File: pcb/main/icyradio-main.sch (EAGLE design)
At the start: 689 parts, among them CON101 FPC-22P, CON1101 2EDG-2P-5MM-H, CON801 PCIE-X4-EDGE, J101 RJ45_MAG_LED_1G-TE-1-2301994-0, J701 TRSJACK, J702 TRSJACK, J703 TRSJACK, M701 SPH0641LM4H-1, M702 SPH0641LM4H-1, Q101 AO3400, Q1101 AO4805, Q1102 AO3400, Q1103 AO3400, Q1104 AO4805, Q1105 AO4805, Q1106 AO3400, T501 UWB1-85E, T502 UWB1-85E, T503 UWB1-85E, T504 UWB1-85E, T505 UWB1-85E, T506 UWB1-85E, T507 UWB1-85E, T508 UWB1-85E, U1001 LTC4313-3, U1002 UPD301C, U1003 MIC2019, U101 MIC2019, U102 RPI-CM4, U1101 MCP1804-3302, U1102 LT7182S, U1201 ADM7172ACPZ-5.0, U1202 ADM7171ACPZ-1.3, U1203 ADM7171ACPZ-3.3, U1204 MIC23159, U1205 MIC5166, U1206 ADM7171ACPZ-1.3, U1207 ADM7171ACPZ-3.3, U1208 MIC23159, U1209 MIC23155, U1210 ADP7142AUJZ-3.3, U1211 ADP150UJZ-1.8, U201 XC7A100TFGG484, U301 MT41K256M16TW-125, U302 MT41K256M16TW-125, U303 DSC1203DA3-333M3333, U401 AD9361, U402 LTC6957-3, U403 TG2520SMN-40.0000M, U501 MIC2019, U502 MIC2019, U503 MIC2019, U504 MIC2019, U505 ADL5601, U506 ADL5601, U601 8V97003, U701 ADAU1372, U901 74LVC1G157, U902 DSB321SDA, U903 SI5351C-B-GM

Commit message: PCB Work
Signed-off-by: João Silva <jgc3silva@gmail.com>
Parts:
- removed R1122, R1123: 10K Ohms, Resistor:RESISTOR-0402
- added C1: 100nF, Capacitor:CAPACITOR-0402
- added D2, D3, D4: LED0603, LED:LED0603
- added R1: 22 Ohms, Resistor:RESISTOR-0402
- added R10, R8, R9: 1K Ohms, Resistor:RESISTOR-0402
- added R2: 2.4K Ohms, Resistor:RESISTOR-0402
- added R3, R4, R5, R6, R7: 4.7K Ohms, Resistor:RESISTOR-0402
- added U1: SST26VF064B, Microchip:SST26VF064B
- C102, C1114, C1126, C1128, C1213, C1214, C1216, C1217, C1218, C1219, C1220, C1222, C1233, C1234, C1235, C1236, C1238, C1239, C1241, C1242, C1254, C1255, C410, C534, C535, C605, C608, C611, C612, C613, C701, C706, C708, C721, C722: device Capacitor:CAPACITOR-0603 -> Capacitor:CAPACITOR-0402
- C1259: value 4.7uF -> 10uF; device Capacitor:CAPACITOR-0603 -> Capacitor:CAPACITOR-0402
- R1210, R1215, R1216, R401: device Resistor:RESISTOR-0603 -> Resistor:RESISTOR-0402
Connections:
- net N$124 renamed VIN_REG_WP
- net N$125 renamed VIN_REG_RUN0
- net N$19 renamed VIN_REG_ASEL
- removed net !1V0_FAULT: R1123.1, U1102.1.!FAULT
- removed net !5V0_FAULT: R1122.1, U1102.0.!FAULT
- new net !FPGA_FLASH_CS: R2.1, U1.!CS!, U201.BANK14.IO_L6P/T0/!FCS
- new net !FPGA_INIT: D4.A, R10.1, R6.1, U201.BANK0-CFG.!INIT
- new net !FPGA_PROGRAM: R7.1, TC201-9(TRST).S, U201.BANK0-CFG.!PROGRAM
- new net FPGA_DONE: D3.A, R9.1, U201.BANK0-CFG.DONE
- new net FPGA_FLASH_IO0: U1.MOSI/IO0, U201.BANK14.IO_L1P/T0/D0/MOSI
- new net FPGA_FLASH_IO1: U1.MISO/IO1, U201.BANK14.IO_L1N/T0/D1/DIN
- new net FPGA_FLASH_IO2: R3.1, U1.!WP!/IO2, U201.BANK14.IO_L2P/T0/D2
- new net FPGA_FLASH_IO3: R4.1, U1.!HOLD!/IO3, U201.BANK14.IO_L2N/T0/D3
- new net FPGA_FLASH_SCK: U1.SCK, U201.BANK0-CFG.CCLK, U201.BANK14.IO_L23P/T3/A3/D19
- new net FPGA_JTAG_EN: R5.2, TC201-10(!RESET!).S, U201.BANK0-CFG.M2
- new net N$19: D2.A, R8.1
- new net TRX_SYNC_IN: R1.2, U201.BANK16.IO_L15P/T2_DQS, U401.INTERFACE.SYNC_IN
- net 2V5: now also U201.BANK16.IO_25, U201.BANK16.IO_L18N/T2, U201.BANK16.IO_L5N/T0, U201.BANK16.IO_L6N/T0/VREF
- net 3V3: now also C1.C1, R10.2, R2.2, R3.2, R4.2, R6.2, R7.2, R9.2, U1.VCC, U201.BANK0-CFG.M0
- net 3V5_VIN_REG_DRVCC: now also U1102.0.!FAULT, U1102.1.!FAULT; no longer R1122.2, R1123.2
- net GND: now also C1.C2, D2.C, D3.C, D4.C, R5.1, U1.GND, U201.BANK0-CFG.DXN, U201.BANK0-CFG.DXP, U201.BANK0-CFG.M1, U201.BANK14.IO_L3P/T0_DQS/!PUDC, U201.BANK15.IO_L10P/T1/AD11P, U201.BANK15.IO_L12N/T1/MRCC, U201.BANK15.IO_L18N/T2/A23, U201.BANK15.IO_L8P/T1/AD10P; no longer U401.INTERFACE.SYNC_IN
- net TRX_CTRL_OUT3: now also U201.BANK16.IO_L12P/T1/MRCC; no longer U201.BANK16.IO_L15N/T2_DQS
- net TRX_ENABLE: now also U201.BANK16.IO_L2P/T0; no longer U201.BANK16.IO_L15P/T2_DQS
- net TRX_EN_AGC: now also U201.BANK16.IO_0; no longer U201.BANK16.IO_L2P/T0
- net TRX_TX/!RX: now also U201.BANK16.IO_L1N/T0; no longer U201.BANK16.IO_0
- net VBUS: now also Q1101.2.D; no longer Q1101.1.D
- net VIN: now also Q1101.1.D; no longer Q1101.2.D
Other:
- moved on the sheet: Q1101.1, Q1101.2, R1119, R1120, TC201-1(VTARGET), U201.BANK0-CFG, U201.BANK0-XADC

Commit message: PCB Work
Signed-off-by: João Silva <jgc3silva@gmail.com>
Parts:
- added C2: 1uF, Capacitor:CAPACITOR-0402
- added CON1: FPC-22P, Generic Connector:FPC-22P
- added R11, R12: 2.2K Ohms, Resistor:RESISTOR-0402
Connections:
- net CM4_CAM_SCL renamed CM4_CAM1_SCL
- net CM4_CAM_SDA renamed CM4_CAM1_SDA
- net N$100 renamed SYNTH_RFOUTB_ACC_N
- net N$102 renamed SYNTH_RFOUTA_ACC_N
- net N$103 renamed SYNTH_RFOUTA_BIAS
- net N$104 renamed SYNTH_RFOUTA_N
- net N$105 renamed SYNTH_VTUNE
- net N$106 renamed SYNTH_RFOUTA_P
- net N$107 renamed SYNTH_RFOUTB_N
- net N$108 renamed SYNTH_RFOUTB_P
- net N$109 renamed SYNTH_CPOUT
- net N$33 renamed PCIE_SLOT_TX1_ACC_N
- net N$34 renamed PCIE_SLOT_TX1_ACC_P
- net N$35 renamed PCIE_SLOT_RX1_ACC_N
- net N$41 renamed PCIE_SLOT_RX1_ACC_P
- net N$43 renamed SYNTH_CPBIAS
- net N$45 renamed PCIE_SLOT_RX0_ACC_N
- net N$46 renamed PCIE_SLOT_RX0_ACC_P
- net N$51 renamed PCIE_CM4_RX_ACC_N
- net N$53 renamed PCIE_CM4_RX_ACC_P
- net N$63 renamed PCIE_SLOT_TX0_ACC_N
- net N$65 renamed PCIE_SLOT_TX0_ACC_P
- net N$68 renamed PCIE_CM4_TX_ACC_N
- net N$69 renamed PCIE_CM4_TX_ACC_P
- net N$75 renamed SYNTH_VREGVCO1
- net N$76 renamed SYNTH_VREGVCO2
- net N$77 renamed SYNTH_VREFVCO1
- net N$84 renamed SYNTH_VREFVCO2
- net N$85 renamed SYNTH_RFOUTB_BIAS
- net N$86 renamed SYNTH_RFOUTA_ACC_P
- net N$88 renamed SYNTH_REFIN_P
- net N$89 renamed SYNTH_REFIN_N
- net N$99 renamed SYNTH_RFOUTB_ACC_P
- new net CM4_CAM0_CSI_C_N: CON1-15.S, U102.CSI0.CAM_C_N
- new net CM4_CAM0_CSI_C_P: CON1-14.S, U102.CSI0.CAM_C_P
- new net CM4_CAM0_CSI_D0_N: CON1-21.S, U102.CSI0.CAM_D0_N
- new net CM4_CAM0_CSI_D0_P: CON1-20.S, U102.CSI0.CAM_D0_P
- new net CM4_CAM0_CSI_D1_N: CON1-18.S, U102.CSI0.CAM_D1_N
- new net CM4_CAM0_CSI_D1_P: CON1-17.S, U102.CSI0.CAM_D1_P
- new net CM4_CAM0_SCL: CON1-3.S, R12.1, U102.GPIO.GPIO1
- new net CM4_CAM0_SDA: CON1-2.S, R11.1, U102.GPIO.GPIO0
- net 3V3_CM4: now also C2.C1, CON1-1.S, R11.2, R12.2
- net CM4_CAM_GPIO: now also CON1-6.S
- net GND: now also C2.C2, CON1-10.S, CON1-13.S, CON1-16.S, CON1-19.S, CON1-22.S, CON1-4.S, CON1-7.S
- net TRX_DATA_CLK: now also U201.BANK15.IO_L13P/T2/MRCC; no longer U201.BANK15.IO_L12P/T1/MRCC
- net TRX_FB_CLK: now also U201.BANK15.IO_L12P/T1/MRCC; no longer U201.BANK15.IO_L13P/T2/MRCC
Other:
- note added: "1V8"
- note added: "CFGBVS = 1 -> Bank 0 at 3V3"
- note added: "DONE LED should light up after FPGA configuration. DONE LED is also controllable through STARTUPE2 primitive"
- note added: "Flash SCK is connecterd to CCLK for initial configuration, and also to a dedicated IO, to be used in the design at full speed."
- note added: "INIT LED should light up after FPGA housekeeping (during configuration)"
- note added: "It seems PTP is only working on one of these pins. To be tested in hardware."
- note added: "M[2:0} = 0b001 -> Boot from SPI Flash M[2:0} = 0b101 -> Boot from JTAG"
- note added: "Pullups as per Xillinx recommendation"
- moved on the sheet: D101, D102, Q101, R101, R104, R105, R106, R107, R110, TP13, TP14, U102.GPIO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

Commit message: PCB Work
Signed-off-by: João Silva <jgc3silva@gmail.com>
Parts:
- added C3: 1uF, Capacitor:CAPACITOR-0402
- added C4: 100nF, Capacitor:CAPACITOR-0402
- added FB1: 1uH, Inductor:FERRITE-0603
- added R13: 49.9 Ohms, Resistor:RESISTOR-0402
- R902, R904: value 100K Ohms -> 10K Ohms
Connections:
- new net N$34: C902.C1, C904.C1, C905.C1, FB1.2, U903.VDDOA, U903.VDDOB, U903.VDDOC, U903.VDDOD
- new net SYNTH_REF_CLK: C601.C1, R13.2
- net 3V3: now also C3.C1, FB1.1; no longer C902.C1, C904.C1, C905.C1, U903.VDDOA, U903.VDDOB, U903.VDDOC, U903.VDDOD
- net EXT_CLK_OUT: now also R912.1; no longer R911.1
- net GND: now also C3.C2, C4.C2, R13.1
- net SYNTH_REFIN_N: now also C4.C1
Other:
- moved on the sheet: C601, C902, C904, C905, C906, C907, C908, R601, R602, R603, R604, R605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

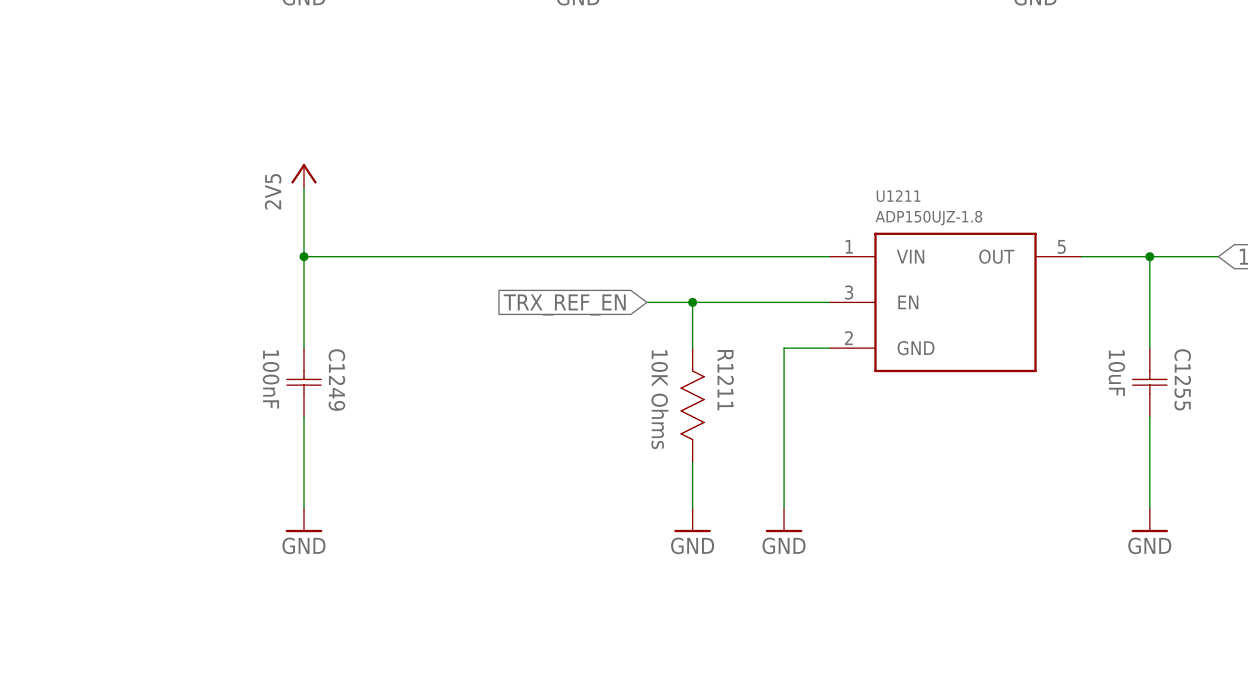
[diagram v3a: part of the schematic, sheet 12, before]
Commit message: Start DDR routing
Signed-off-by: João Silva <jgc3silva@gmail.com>
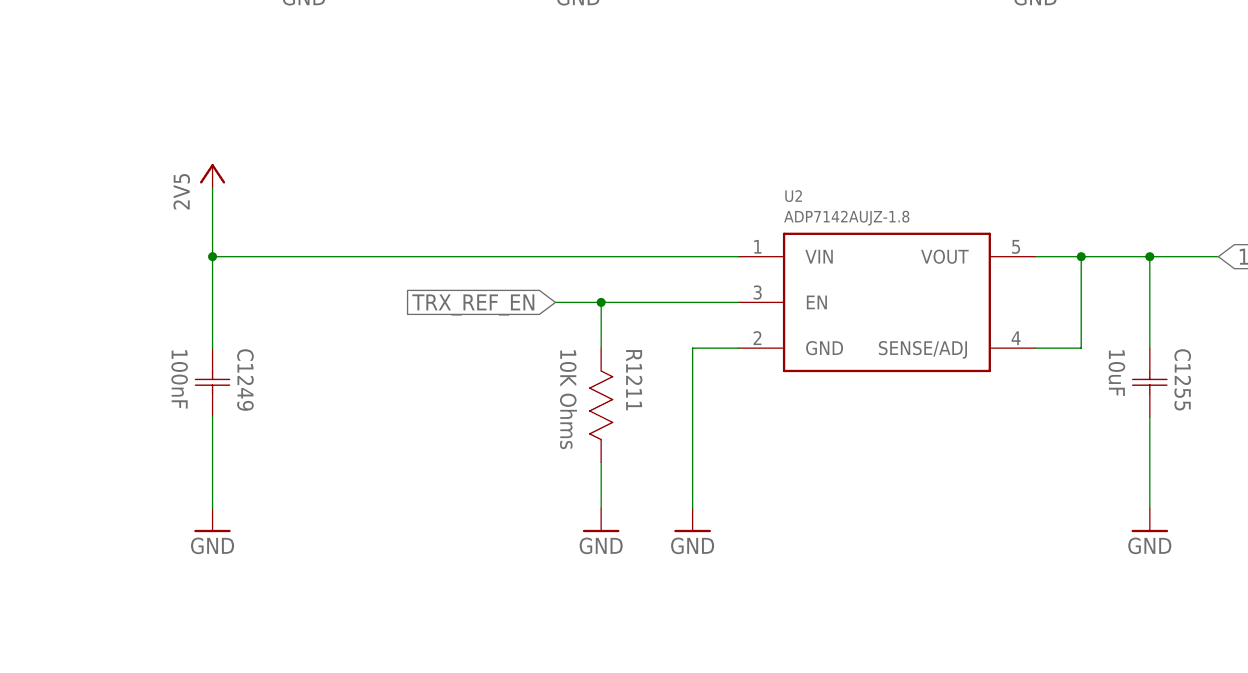
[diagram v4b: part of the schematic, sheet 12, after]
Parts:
- removed U1211: ADP150UJZ-1.8, Analog Devices:ADP150UJZ-1.8
- added U2: ADP7142AUJZ-1.8, Analog Devices:ADP7142AUJZ-1.8
- L1201, L1202, L1203, L1204, L1205: REF_COILCRAFT XGL3515-222ME -> (none)
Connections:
- new net CM4_UART_RXD: U102.GPIO.GPIO15
- new net CM4_UART_TXD: U102.GPIO.GPIO14
- new net CM4_WAKE: U102.GPIO.GPIO3
- net 1V8_TRX_REF: now also U2.SENSE/ADJ, U2.VOUT; no longer U1211.OUT
- net 2V5: now also U2.VIN; no longer U1211.VIN
- net GND: now also U2.GND; no longer U1211.GND
- net TRX_REF_EN: now also U2.EN; no longer U1211.EN
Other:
- moved on the sheet: C1249, R1211

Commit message: Remove second DDR3 chip as it was impossible to route with a 6-layer board Update HDL project to reflect hardware changes
Signed-off-by: João Silva <jgc3silva@gmail.com>
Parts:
- removed R301: 240 Ohms, Resistor:RESISTOR-0402
- removed R326: 40.2 Ohms, Resistor:RESISTOR-0402
- removed U301: MT41K256M16TW-125, Micron:MT41K256M16TW-125
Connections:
- removed net !DDR3_CS: R324.1, U201.BANK34.IO_L18N/T2, U301.!CS, U302.!CS
- removed net DDR3_DM2: U201.BANK35.IO_L19P/T3, U302.LDM
- removed net DDR3_DM3: U201.BANK34.IO_L1P/T0, U302.UDM
- removed net DDR3_DQ16: U201.BANK35.IO_L20P/T3, U302.DQ0
- removed net DDR3_DQ17: U201.BANK35.IO_L20N/T3, U302.DQ1
- removed net DDR3_DQ18: U201.BANK35.IO_L22P/T3, U302.DQ2
- removed net DDR3_DQ19: U201.BANK35.IO_L22N/T3, U302.DQ3
- removed net DDR3_DQ20: U201.BANK35.IO_L23P/T3, U302.DQ4
- removed net DDR3_DQ21: U201.BANK35.IO_L23N/T3, U302.DQ5
- removed net DDR3_DQ22: U201.BANK35.IO_L24P/T3, U302.DQ6
- removed net DDR3_DQ23: U201.BANK35.IO_L24N/T3, U302.DQ7
- removed net DDR3_DQ24: U201.BANK34.IO_L1N/T0, U302.DQ8
- removed net DDR3_DQ25: U201.BANK34.IO_L2P/T0, U302.DQ9
- removed net DDR3_DQ26: U201.BANK34.IO_L2N/T0, U302.DQ10
- removed net DDR3_DQ27: U201.BANK34.IO_L4P/T0, U302.DQ11
- removed net DDR3_DQ28: U201.BANK34.IO_L4N/T0, U302.DQ12
- removed net DDR3_DQ29: U201.BANK34.IO_L5P/T0, U302.DQ13
- removed net DDR3_DQ30: U201.BANK34.IO_L5N/T0, U302.DQ14
- removed net DDR3_DQ31: U201.BANK34.IO_L6P/T0, U302.DQ15
- removed net DDR3_DQS2_N: U201.BANK35.IO_L21N/T3_DQS, U302.!LDQS
- removed net DDR3_DQS2_P: U201.BANK35.IO_L21P/T3_DQS, U302.LDQS
- removed net DDR3_DQS3_N: U201.BANK34.IO_L3N/T0_DQS, U302.!UDQS
- removed net DDR3_DQS3_P: U201.BANK34.IO_L3P/T0_DQS, U302.UDQS
- removed net N$54: R301.2, U301.ZQ
- net !DDR3_CAS: now also R329.1; no longer R323.1, U301.!CAS
- net !DDR3_RAS: now also R325.1; no longer R328.1, U301.!RAS
- net !DDR3_RESET: now also U201.BANK34.IO_L13P/T2/MRCC; no longer U201.BANK35.IO_L18N/T2, U301.!RESET
- net !DDR3_WE: now also R324.1; no longer R327.1, U301.!WE
- net 0V675_DDR3_VREF: no longer U301.VREFCA, U301.VREFDQ
- net 0V675_DDR3_VTT: no longer R326.2
- net 1V35: no longer U301.VDD, U301.VDDQ
- net DDR3_A0: no longer U301.A0
- net DDR3_A1: no longer U301.A1
- net DDR3_A10: no longer U301.A10/AP
- net DDR3_A11: no longer U301.A11
- net DDR3_A12: no longer U301.A12/!BC
- net DDR3_A13: no longer U301.A13
- net DDR3_A14: no longer U301.A14
- net DDR3_A2: no longer U301.A2
- net DDR3_A3: no longer U301.A3
- net DDR3_A4: no longer U301.A4
- net DDR3_A5: no longer U301.A5
- net DDR3_A6: no longer U301.A6
- net DDR3_A7: no longer U301.A7
- net DDR3_A8: no longer U301.A8
- net DDR3_A9: no longer U301.A9
- net DDR3_BA0: now also R323.1; no longer R326.1, U301.BA0
- net DDR3_BA1: now also R327.1; no longer R330.1, U301.BA1
- net DDR3_BA2: now also R322.1; no longer R325.1, U301.BA2
- net DDR3_CLK_EN: now also R330.1, U201.BANK34.IO_L18N/T2; no longer R329.1, U201.BANK34.IO_L19P/T3, U301.CKE
- net DDR3_CLK_IN_N: now also U201.BANK35.IO_L12N/T1/MRCC; no longer U201.BANK34.IO_L13N/T2/MRCC
- net DDR3_CLK_IN_P: now also U201.BANK35.IO_L12P/T1/MRCC; no longer U201.BANK34.IO_L13P/T2/MRCC
- net DDR3_CLK_N: no longer U301.!CK
- net DDR3_CLK_P: no longer U301.CK
- net DDR3_DM0: now also U201.BANK35.IO_L19P/T3, U302.LDM; no longer U201.BANK35.IO_L7P/T1/AD6P, U301.LDM
- net DDR3_DM1: now also U201.BANK34.IO_L1P/T0, U302.UDM; no longer U201.BANK35.IO_L16P/T2, U301.UDM
- net DDR3_DQ0: now also U201.BANK35.IO_L20P/T3, U302.DQ0; no longer U201.BANK35.IO_L7N/T1/AD6N, U301.DQ0
- net DDR3_DQ1: now also U201.BANK35.IO_L20N/T3, U302.DQ1; no longer U201.BANK35.IO_L8P/T1/AD14P, U301.DQ1
- net DDR3_DQ10: now also U201.BANK34.IO_L2N/T0, U302.DQ10; no longer U201.BANK35.IO_L14P/T2/SRCC, U301.DQ10
- net DDR3_DQ11: now also U201.BANK34.IO_L4P/T0, U302.DQ11; no longer U201.BANK35.IO_L14N/T2/SRCC, U301.DQ11
- net DDR3_DQ12: now also U201.BANK34.IO_L4N/T0, U302.DQ12; no longer U201.BANK35.IO_L16N/T2, U301.DQ12
- net DDR3_DQ13: now also U201.BANK34.IO_L5P/T0, U302.DQ13; no longer U201.BANK35.IO_L17P/T2, U301.DQ13
- net DDR3_DQ14: now also U201.BANK34.IO_L5N/T0, U302.DQ14; no longer U201.BANK35.IO_L17N/T2, U301.DQ14
- net DDR3_DQ15: now also U201.BANK34.IO_L6P/T0, U302.DQ15; no longer U201.BANK35.IO_L18P/T2, U301.DQ15
- net DDR3_DQ2: now also U201.BANK35.IO_L22P/T3, U302.DQ2; no longer U201.BANK35.IO_L8N/T1/AD14N, U301.DQ2
- net DDR3_DQ3: now also U201.BANK35.IO_L22N/T3, U302.DQ3; no longer U201.BANK35.IO_L10P/T1/AD15P, U301.DQ3
- net DDR3_DQ4: now also U201.BANK35.IO_L23P/T3, U302.DQ4; no longer U201.BANK35.IO_L10N/T1/AD15N, U301.DQ4
- net DDR3_DQ5: now also U201.BANK35.IO_L23N/T3, U302.DQ5; no longer U201.BANK35.IO_L11P/T1/SRCC, U301.DQ5
- net DDR3_DQ6: now also U201.BANK35.IO_L24P/T3, U302.DQ6; no longer U201.BANK35.IO_L11N/T1/SRCC, U301.DQ6
- net DDR3_DQ7: now also U201.BANK35.IO_L24N/T3, U302.DQ7; no longer U201.BANK35.IO_L12P/T1/MRCC, U301.DQ7
- net DDR3_DQ8: now also U201.BANK34.IO_L1N/T0, U302.DQ8; no longer U201.BANK35.IO_L13P/T2/MRCC, U301.DQ8
- net DDR3_DQ9: now also U201.BANK34.IO_L2P/T0, U302.DQ9; no longer U201.BANK35.IO_L13N/T2/MRCC, U301.DQ9
- net DDR3_DQS0_N: now also U201.BANK35.IO_L21N/T3_DQS, U302.!LDQS; no longer U201.BANK35.IO_L9N/T1_DQS/AD7N, U301.!LDQS
- net DDR3_DQS0_P: now also U201.BANK35.IO_L21P/T3_DQS, U302.LDQS; no longer U201.BANK35.IO_L9P/T1_DQS/AD7P, U301.LDQS
- net DDR3_DQS1_N: now also U201.BANK34.IO_L3N/T0_DQS, U302.!UDQS; no longer U201.BANK35.IO_L15N/T2_DQS, U301.!UDQS
- net DDR3_DQS1_P: now also U201.BANK34.IO_L3P/T0_DQS, U302.UDQS; no longer U201.BANK35.IO_L15P/T2_DQS, U301.UDQS
- net DDR3_ODT: now also R328.1, U201.BANK34.IO_L19P/T3; no longer R322.1, U201.BANK34.IO_L20P/T3, U301.ODT
- net GND: now also U302.!CS; no longer R301.1, U301.VSS, U301.VSSQ
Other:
- moved on the sheet: C348, C349, C350, C351, C352, R304, R305, R306, R307, R308, R309, R310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
